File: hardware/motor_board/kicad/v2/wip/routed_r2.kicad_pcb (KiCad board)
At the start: 4 copper layers, 85 x 35 mm, 232 parts, among them J1 BOOMELE_1.27-2x10P, J2 BM06B-SRSS-TB, J3 BM06B-SRSS-TB, J4 B5B-XH-A, Q1 HYG015N04LS1C2, Q2 HYG015N04LS1C2, Q3 HYG015N04LS1C2, Q4 HYG015N04LS1C2, Q5 HYG015N04LS1C2, Q6 HYG015N04LS1C2, Q7 HYG015N04LS1C2, Q8 HYG015N04LS1C2, U1 STM32G474RET6, U10 SN74LVC3G17DCUR, U11 TPS22945DCKR, U12 TPS22945DCKR, U13 LM74502DDFR, U14 74LVC1G17SE-7, U2 DRV8323RHRGZR, U3 DRV8316CRRGFR, U4 DRV8316CRRGFR, U5 AP2112K-3.3TRG1, U6 SN74LVC08ABQAR, U7 INA239AIDGSR, U8 BQ76907RGRR, U9 SN74LVC3G17DCUR

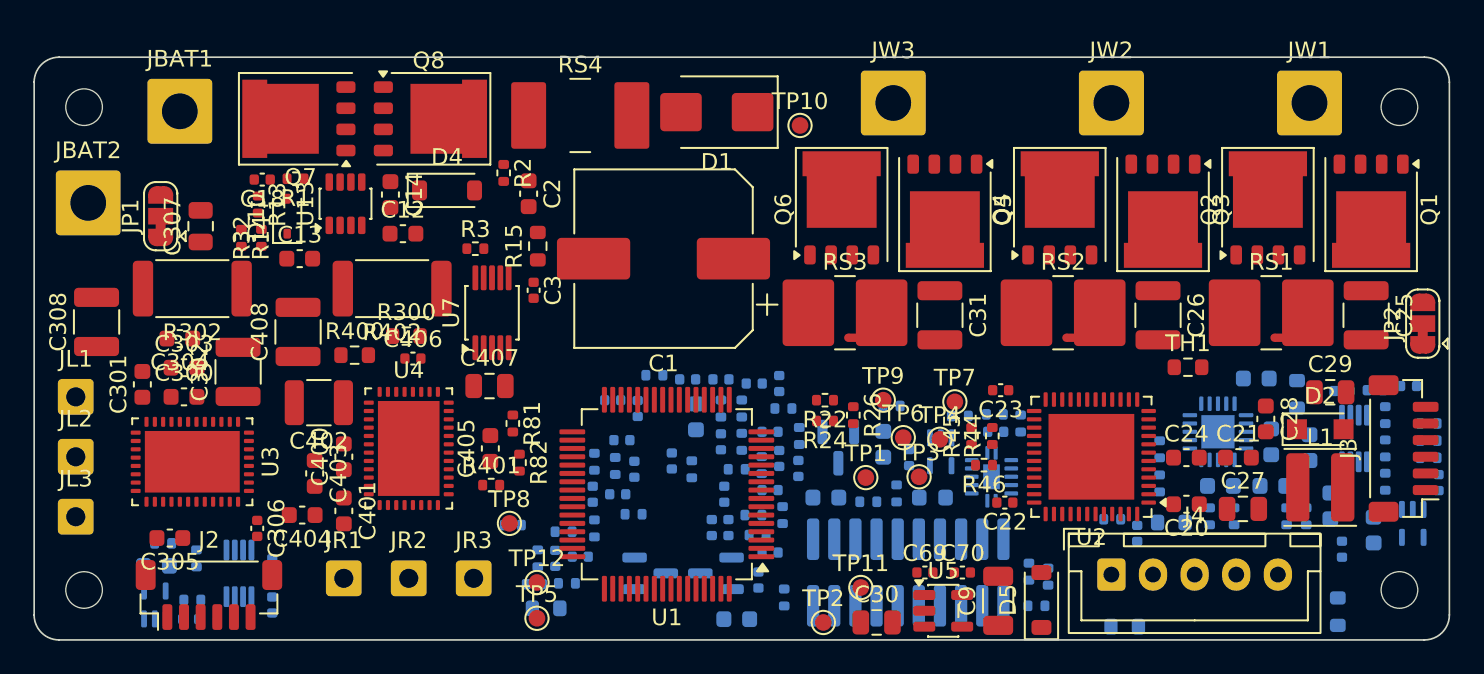
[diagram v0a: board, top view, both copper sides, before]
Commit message: v2 rear band second pass (r2): J1 behind the MCU, J4 + BMS rear-right, buck east of U2, J3 +1.75 mm east; stages r2_u2east/bms/senr/main/gnd; routed_r2 DRC 0 errors (with motor_board.kicad_dru), 41 signal/rail opens, L2 one piece, L3 GND 33 pieces; router via-pitch + via-to-PTH rules; r2/ eval tools
Co-Authored-By: Claude Opus 5.5 (1M context) <noreply@anthropic.com>
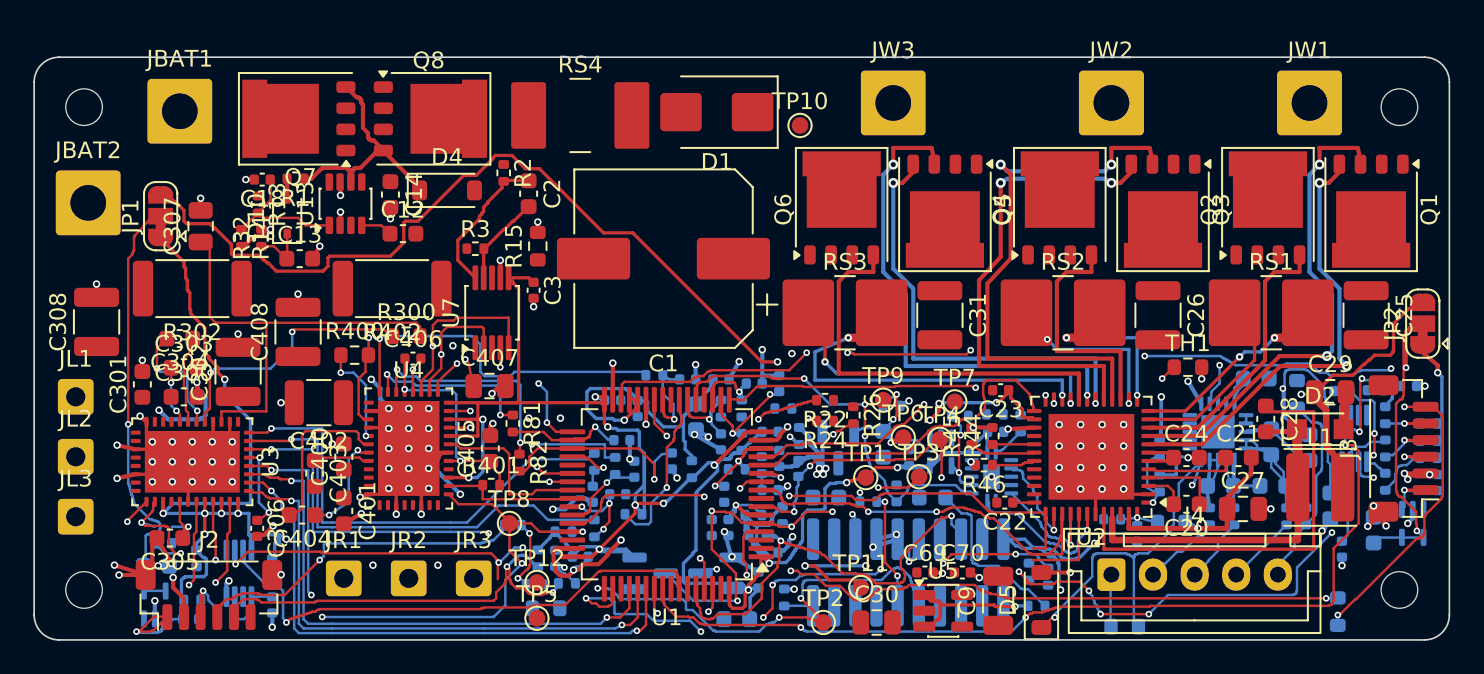
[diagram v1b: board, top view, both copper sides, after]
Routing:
- net +3V3: track 0.00 -> 233.8 mm, vias 0 -> 23
- net +5V: track 0.00 -> 148.2 mm, vias 0 -> 8
- net GND: track 0.00 -> 130.9 mm, vias 0 -> 138
- net BMS_SCL: track 0.00 -> 60.6 mm, vias 0 -> 7
- net R_MTEMP: track 0.00 -> 60.3 mm, vias 0 -> 6
- net SPI_MOSI: track 0.00 -> 60.1 mm, vias 0 -> 3
- net R_S3: track 0.00 -> 59.9 mm, vias 0 -> 6
- net SPI_SCK: track 0.00 -> 59.8 mm, vias 0 -> 3
- net SPI_MISO: track 0.00 -> 56.9 mm, vias 0 -> 4
- net R_S2: track 0.00 -> 55.2 mm, vias 0 -> 3
- net /power/CELL0: track 0.00 -> 52.0 mm, vias 0 -> 3
- net L_nFAULT: track 0.00 -> 45.1 mm, vias 0 -> 3
- net DRV_OFF: track 0.00 -> 44.8 mm, vias 0 -> 4
- net W_ARM_S: track 0.00 -> 38.6 mm, vias 0 -> 3
- net /mcu/SWCLK: track 0.00 -> 38.1 mm, vias 0 -> 7
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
